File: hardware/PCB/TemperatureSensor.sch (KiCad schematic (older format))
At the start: 0 parts

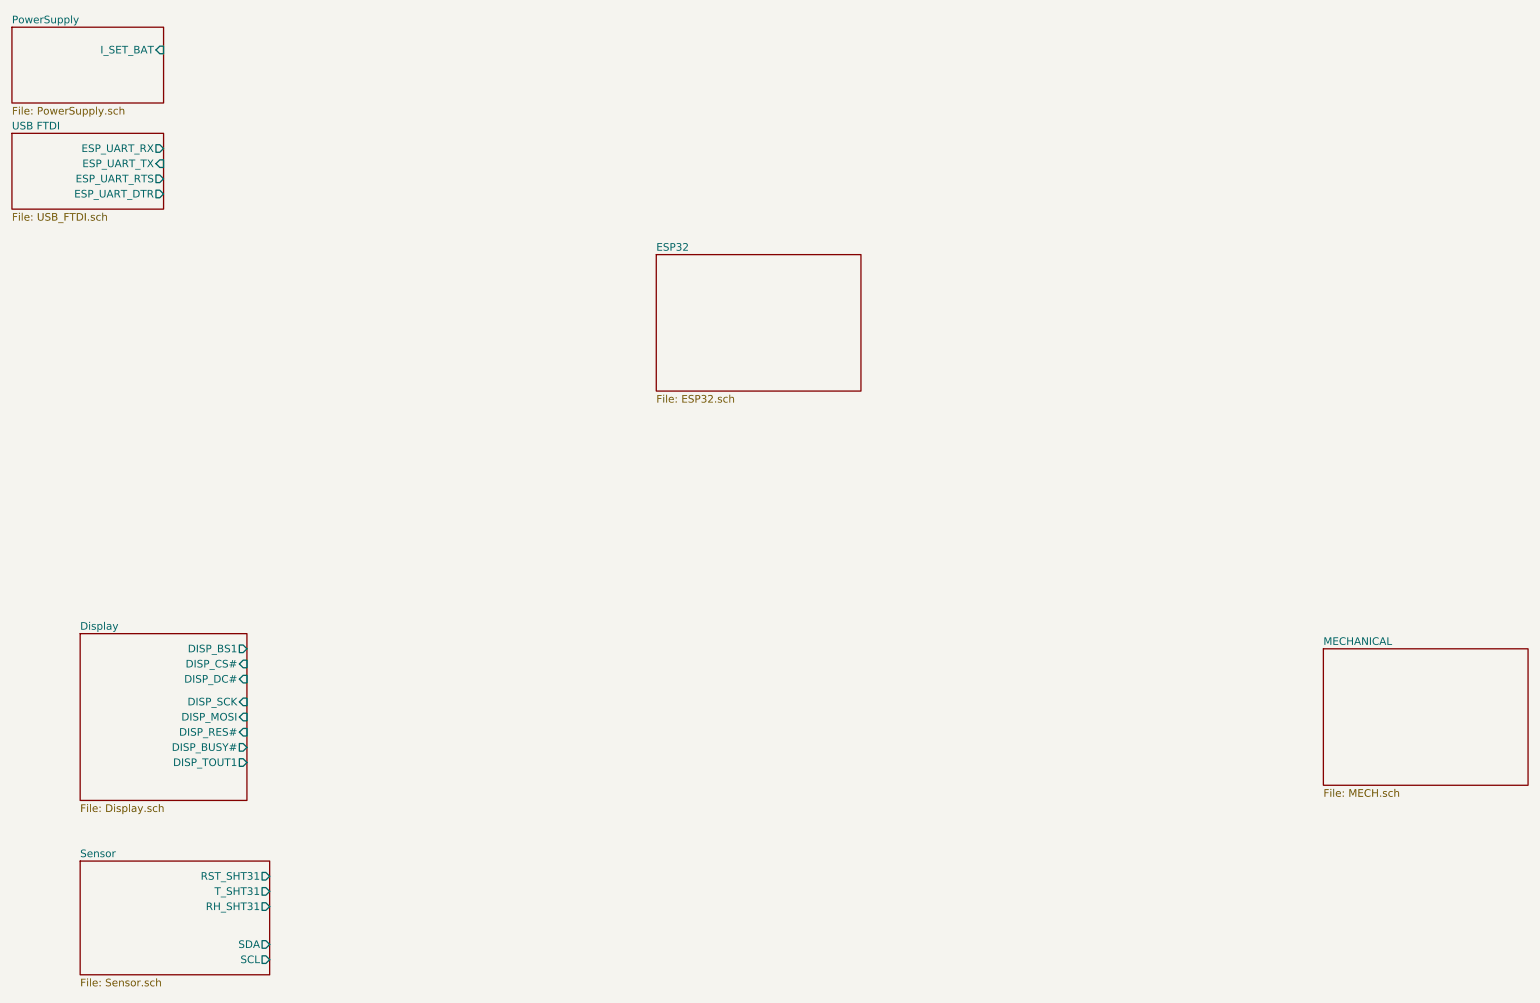
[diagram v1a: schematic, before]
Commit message: Connect ESP32 pins
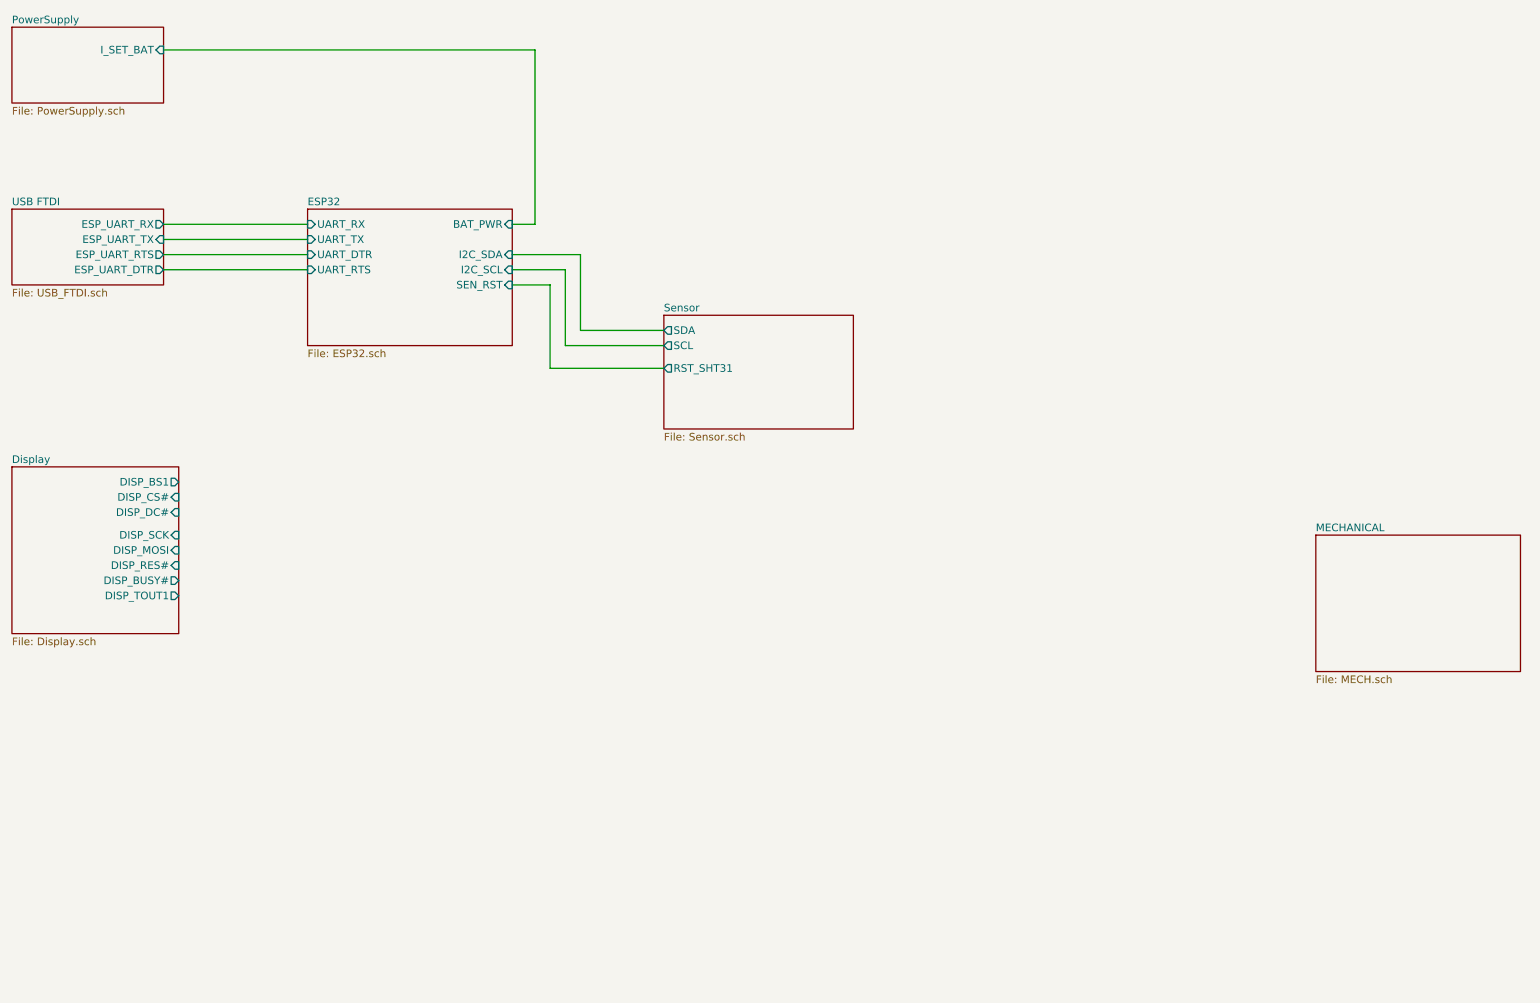
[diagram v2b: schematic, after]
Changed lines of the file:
@@
 $EndSheet
 $Sheet
-S 1450 5000 1100 1100
+S 1000 3900 1100 1100
 U 5FC321F3
 F0 "Display" 50
 F1 "Display.sch" 50
-F2 "DISP_SCK" I R 2550 5450 50
-F3 "DISP_MOSI" I R 2550 5550 50
-F4 "DISP_BS1" O R 2550 5100 50
-F5 "DISP_CS#" I R 2550 5200 50
-F6 "DISP_DC#" I R 2550 5300 50
-F7 "DISP_RES#" I R 2550 5650 50
-F8 "DISP_BUSY#" O R 2550 5750 50
-F9 "DISP_TOUT1" O R 2550 5850 50
+F2 "DISP_SCK" I R 2100 4350 50
+F3 "DISP_MOSI" I R 2100 4450 50
+F4 "DISP_BS1" O R 2100 4000 50
+F5 "DISP_CS#" I R 2100 4100 50
+F6 "DISP_DC#" I R 2100 4200 50
+F7 "DISP_RES#" I R 2100 4550 50
+F8 "DISP_BUSY#" O R 2100 4650 50
+F9 "DISP_TOUT1" O R 2100 4750 50
 $EndSheet
 $Sheet
-S 1450 6500 1250 750
+S 5300 2900 1250 750
 U 5FCF6796
 F0 "Sensor" 50
 F1 "Sensor.sch" 50
-F2 "RST_SHT31" O R 2700 6600 50
-F3 "T_SHT31" O R 2700 6700 50
-F4 "RH_SHT31" O R 2700 6800 50
-F5 "SDA" O R 2700 7050 50
-F6 "SCL" O R 2700 7150 50
+F2 "SDA" O L 5300 3000 50
+F3 "SCL" O L 5300 3100 50
+F4 "RST_SHT31" O L 5300 3250 50
 $EndSheet
 $Sheet
-S 9650 5100 1350 900
+S 9600 4350 1350 900
 U 5FE895CA
 F0 "MECHANICAL" 50
@@
 $EndSheet
 $Sheet
-S 1000 1700 1000 500
+S 1000 2200 1000 500
 U 5FE9624E
 F0 "USB FTDI" 50
 F1 "USB_FTDI.sch" 50
-F2 "ESP_UART_RX" O R 2000 1800 50
-F3 "ESP_UART_TX" I R 2000 1900 50
-F4 "ESP_UART_RTS" O R 2000 2000 50
-F5 "ESP_UART_DTR" O R 2000 2100 50
+F2 "ESP_UART_RX" O R 2000 2300 50
+F3 "ESP_UART_TX" I R 2000 2400 50
+F4 "ESP_UART_RTS" O R 2000 2500 50
+F5 "ESP_UART_DTR" O R 2000 2600 50
 $EndSheet
 $Sheet
-S 5250 2500 1350 900
+S 2950 2200 1350 900
 U 5FCFD0E2
 F0 "ESP32" 50
 F1 "ESP32.sch" 50
+F2 "UART_RTS" I L 2950 2600 50
+F3 "UART_DTR" I L 2950 2500 50
+F4 "UART_RX" I L 2950 2300 50
+F5 "UART_TX" I L 2950 2400 50
+F6 "BAT_PWR" I R 4300 2300 50
+F7 "I2C_SCL" I R 4300 2600 50
+F8 "I2C_SDA" I R 4300 2500 50
+F9 "SEN_RST" I R 4300 2700 50
 $EndSheet
+Wire Wire Line
+	2950 2300 2000 2300
+Wire Wire Line
+	2950 2400 2000 2400
+Wire Wire Line
+	2950 2500 2000 2500
+Wire Wire Line
+	2950 2600 2000 2600
+Wire Wire Line
+	4300 2300 4450 2300
+Wire Wire Line
+	4450 2300 4450 1150
+Wire Wire Line
+	4450 1150 2000 1150
+Wire Wire Line
+	5300 3000 4750 3000
+Wire Wire Line
+	4750 3000 4750 2500
+Wire Wire Line
+	4750 2500 4300 2500
+Wire Wire Line
+	5300 3100 4650 3100
+Wire Wire Line
+	4650 3100 4650 2600
+Wire Wire Line
+	4650 2600 4300 2600
+Wire Wire Line
+	4300 2700 4550 2700
+Wire Wire Line
+	4550 2700 4550 3250
+Wire Wire Line
+	4550 3250 5300 3250
 $EndSCHEMATC

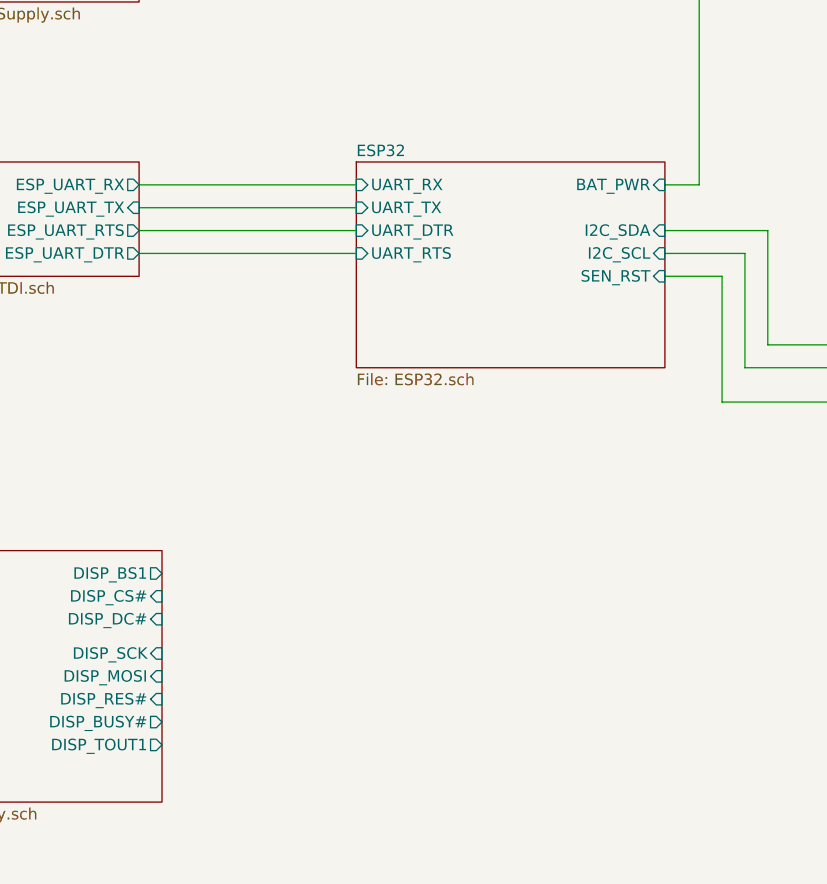
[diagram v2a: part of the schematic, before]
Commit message: Connect Display
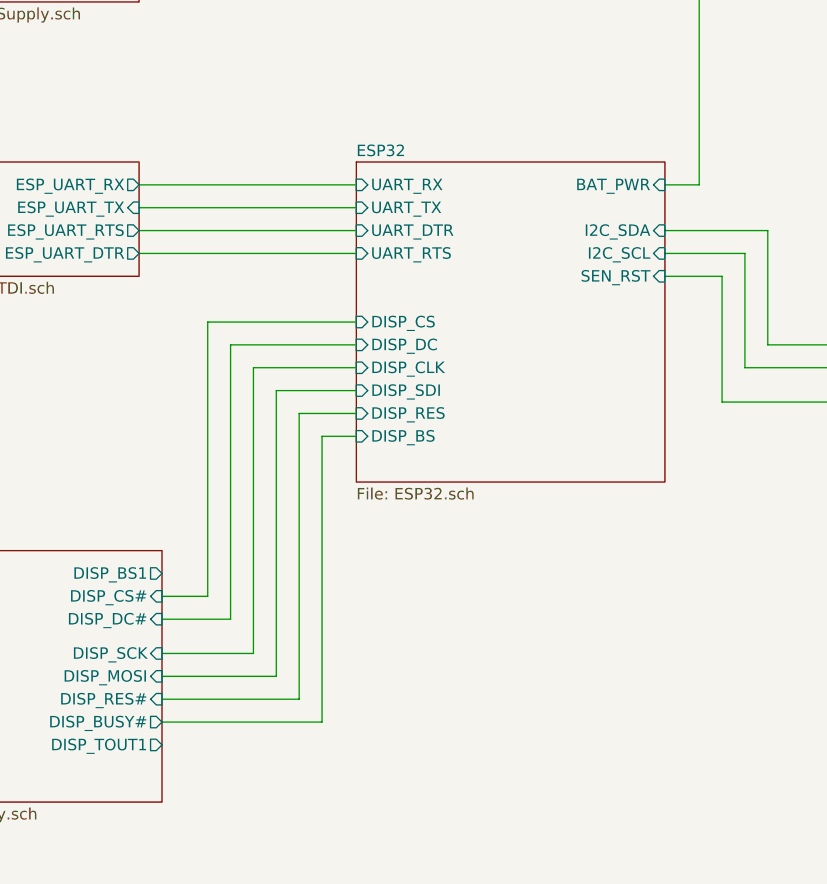
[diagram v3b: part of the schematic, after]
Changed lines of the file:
@@
 $EndSheet
 $Sheet
-S 2950 2200 1350 900
+S 2950 2200 1350 1400
 U 5FCFD0E2
 F0 "ESP32" 50
@@
 F8 "I2C_SDA" I R 4300 2500 50
 F9 "SEN_RST" I R 4300 2700 50
+F10 "DISP_CLK" I L 2950 3100 50
+F11 "DISP_CS" I L 2950 2900 50
+F12 "DISP_SDI" I L 2950 3200 50
+F13 "DISP_DC" I L 2950 3000 50
+F14 "DISP_BS" I L 2950 3400 50
+F15 "DISP_RES" I L 2950 3300 50
 $EndSheet
 Wire Wire Line
@@
 Wire Wire Line
 	4550 3250 5300 3250
+Wire Wire Line
+	2950 3400 2800 3400
+Wire Wire Line
+	2800 3400 2800 4650
+Wire Wire Line
+	2800 4650 2100 4650
+Wire Wire Line
+	2950 3300 2700 3300
+Wire Wire Line
+	2700 3300 2700 4550
+Wire Wire Line
+	2700 4550 2100 4550
+Wire Wire Line
+	2950 3200 2600 3200
+Wire Wire Line
+	2600 3200 2600 4450
+Wire Wire Line
+	2600 4450 2100 4450
+Wire Wire Line
+	2950 3100 2500 3100
+Wire Wire Line
+	2500 3100 2500 4350
+Wire Wire Line
+	2500 4350 2100 4350
+Wire Wire Line
+	2950 3000 2400 3000
+Wire Wire Line
+	2400 3000 2400 4200
+Wire Wire Line
+	2400 4200 2100 4200
+Wire Wire Line
+	2950 2900 2300 2900
+Wire Wire Line
+	2300 2900 2300 4100
+Wire Wire Line
+	2300 4100 2100 4100
 $EndSCHEMATC

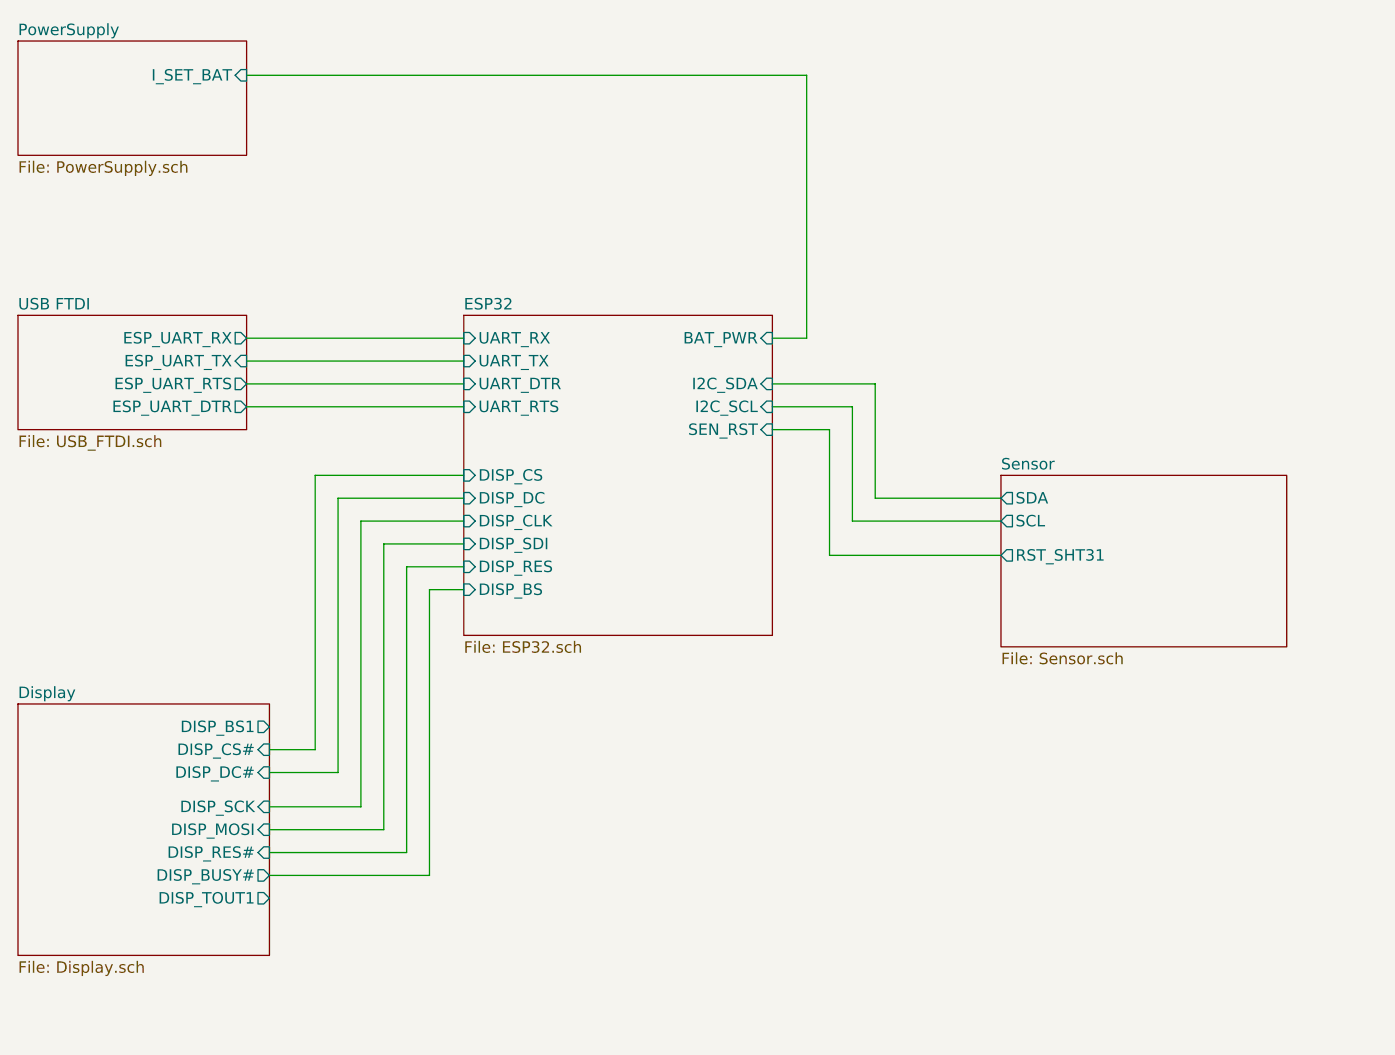
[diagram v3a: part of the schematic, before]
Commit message: correctrts, dtr connection, change spi connections, complete display connection
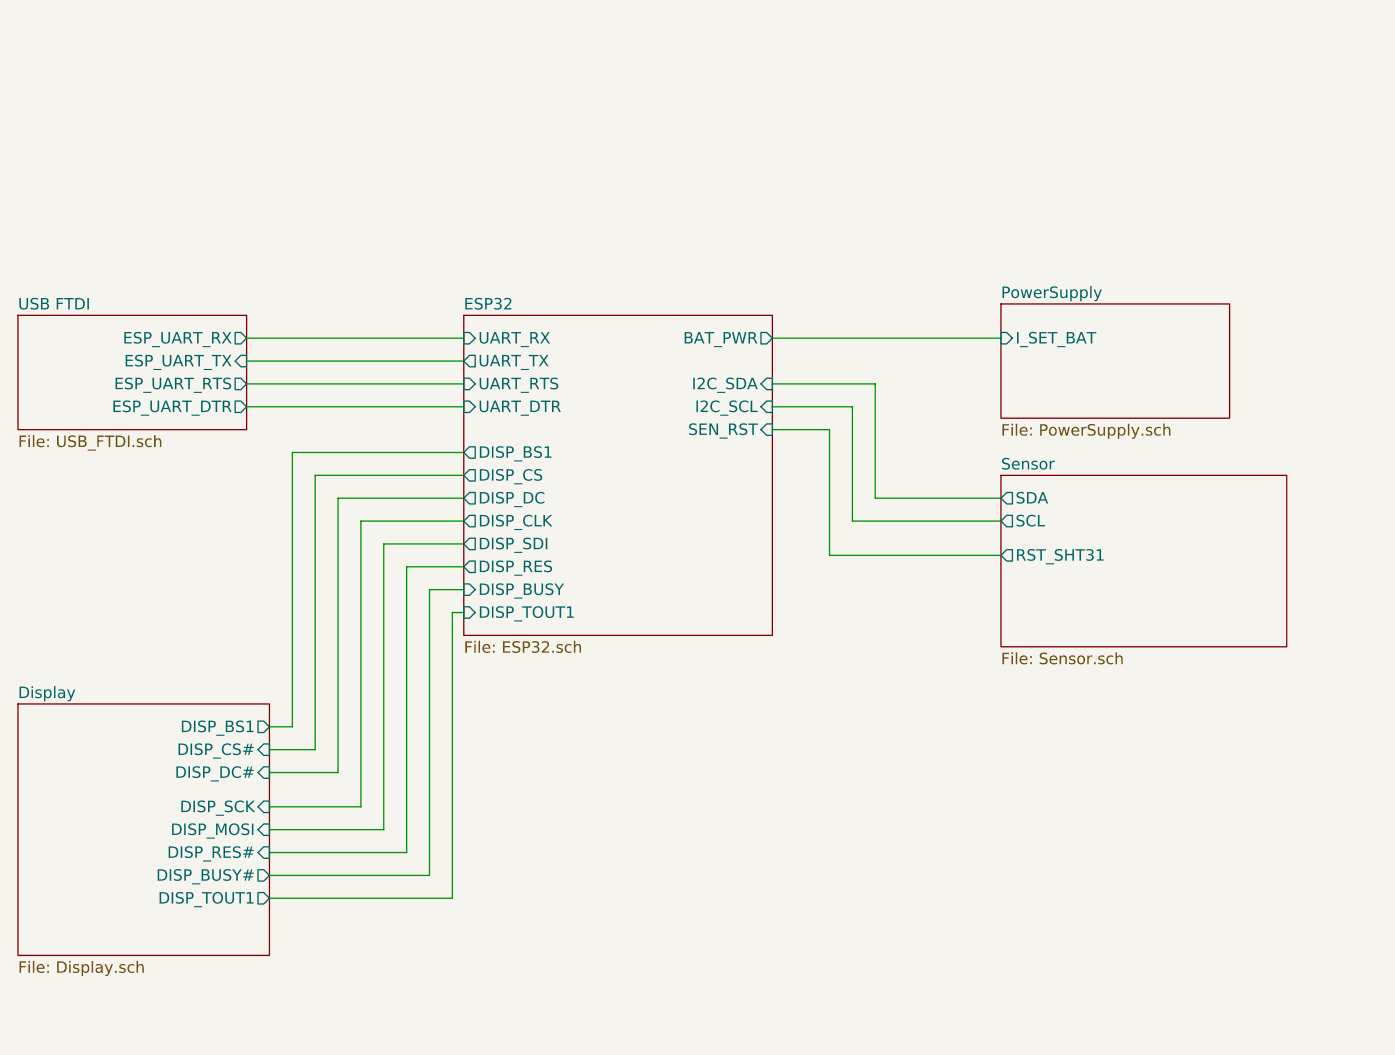
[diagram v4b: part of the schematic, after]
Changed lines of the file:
@@
 $EndDescr
 $Sheet
-S 1000 1000 1000 500
+S 5300 2150 1000 500
 U 5FBFD530
 F0 "PowerSupply" 50
 F1 "PowerSupply.sch" 50
-F2 "I_SET_BAT" I R 2000 1150 50
+F2 "I_SET_BAT" I L 5300 2300 50
 $EndSheet
 $Sheet
@@
 F5 "ESP_UART_DTR" O R 2000 2600 50
 $EndSheet
-$Sheet
-S 2950 2200 1350 1400
-U 5FCFD0E2
-F0 "ESP32" 50
-F1 "ESP32.sch" 50
-F2 "UART_RTS" I L 2950 2600 50
-F3 "UART_DTR" I L 2950 2500 50
-F4 "UART_RX" I L 2950 2300 50
-F5 "UART_TX" I L 2950 2400 50
-F6 "BAT_PWR" I R 4300 2300 50
-F7 "I2C_SCL" I R 4300 2600 50
-F8 "I2C_SDA" I R 4300 2500 50
-F9 "SEN_RST" I R 4300 2700 50
-F10 "DISP_CLK" I L 2950 3100 50
-F11 "DISP_CS" I L 2950 2900 50
-F12 "DISP_SDI" I L 2950 3200 50
-F13 "DISP_DC" I L 2950 3000 50
-F14 "DISP_BS" I L 2950 3400 50
-F15 "DISP_RES" I L 2950 3300 50
-$EndSheet
 Wire Wire Line
 	2950 2300 2000 2300
@@
 Wire Wire Line
 	2950 2600 2000 2600
-Wire Wire Line
-	4300 2300 4450 2300
-Wire Wire Line
-	4450 2300 4450 1150
-Wire Wire Line
-	4450 1150 2000 1150
 Wire Wire Line
 	5300 3000 4750 3000
@@
 Wire Wire Line
 	2300 4100 2100 4100
+$Sheet
+S 2950 2200 1350 1400
+U 5FCFD0E2
+F0 "ESP32" 50
+F1 "ESP32.sch" 50
+F2 "UART_RTS" I L 2950 2500 50
+F3 "UART_DTR" I L 2950 2600 50
+F4 "UART_RX" I L 2950 2300 50
+F5 "I2C_SCL" I R 4300 2600 50
+F6 "I2C_SDA" I R 4300 2500 50
+F7 "SEN_RST" I R 4300 2700 50
+F8 "UART_TX" O L 2950 2400 50
+F9 "BAT_PWR" O R 4300 2300 50
+F10 "DISP_CLK" O L 2950 3100 50
+F11 "DISP_CS" O L 2950 2900 50
+F12 "DISP_DC" O L 2950 3000 50
+F13 "DISP_BUSY" I L 2950 3400 50
+F14 "DISP_RES" O L 2950 3300 50
+F15 "DISP_SDI" O L 2950 3200 50
+F16 "DISP_BS1" O L 2950 2800 50
+F17 "DISP_TOUT1" I L 2950 3500 50
+$EndSheet
+Wire Wire Line
+	2100 4000 2200 4000
+Wire Wire Line
+	2200 4000 2200 2800
+Wire Wire Line
+	2200 2800 2950 2800
+Wire Wire Line
+	2100 4750 2900 4750
+Wire Wire Line
+	2900 4750 2900 3500
+Wire Wire Line
+	2900 3500 2950 3500
+Wire Wire Line
+	4300 2300 5300 2300
 $EndSCHEMATC
